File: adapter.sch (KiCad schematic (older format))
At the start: 5 parts, among them CN1 Molex_52602_0579, CN2 CONN_25X2, CN3 CONN_02X22

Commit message: Consolidate all power lines connected on the DC mainboard
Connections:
- net labels removed: +12V_2, +3V3_2, +5V_2, GND2, P.GND, P.GND_2, xA13, xA18, xA21, xB13, xB18, xB21

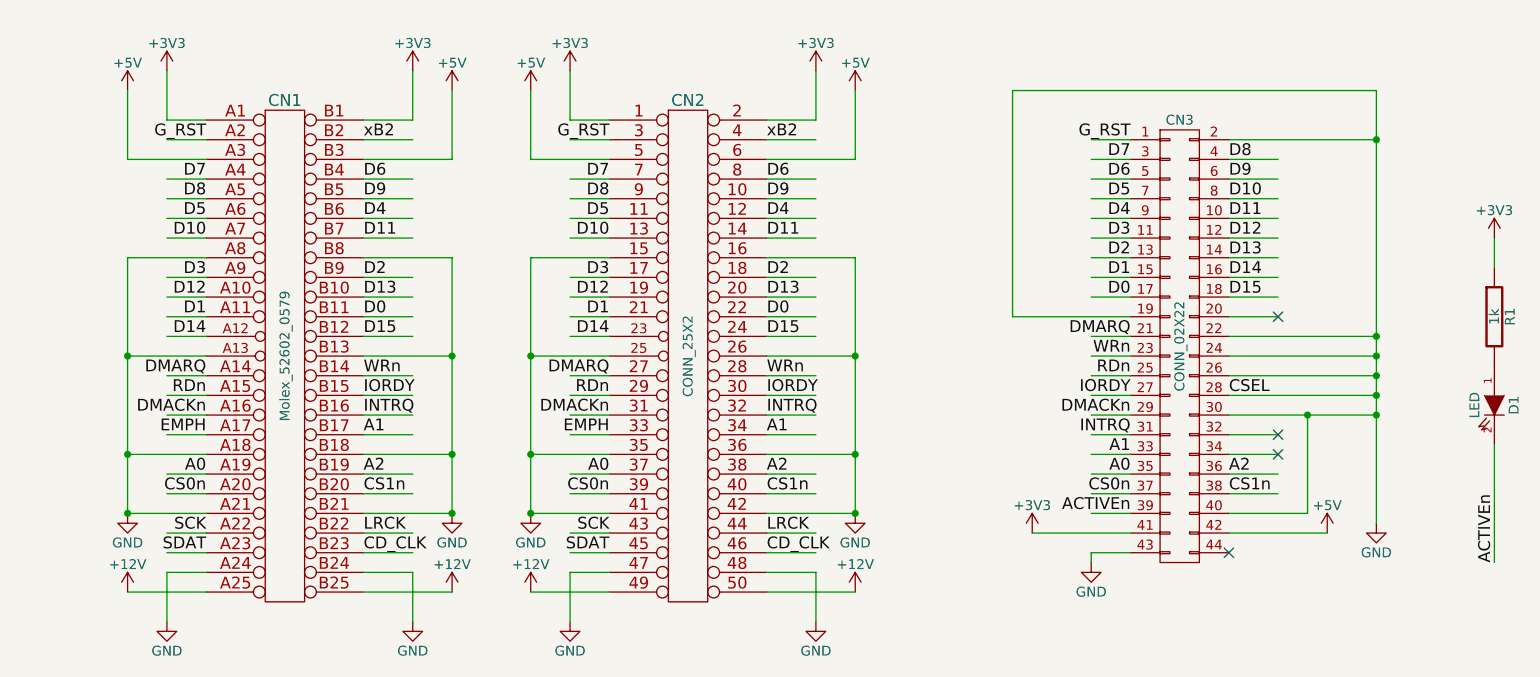
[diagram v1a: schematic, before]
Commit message: Add PWR_FLAG to prevent ERC errors
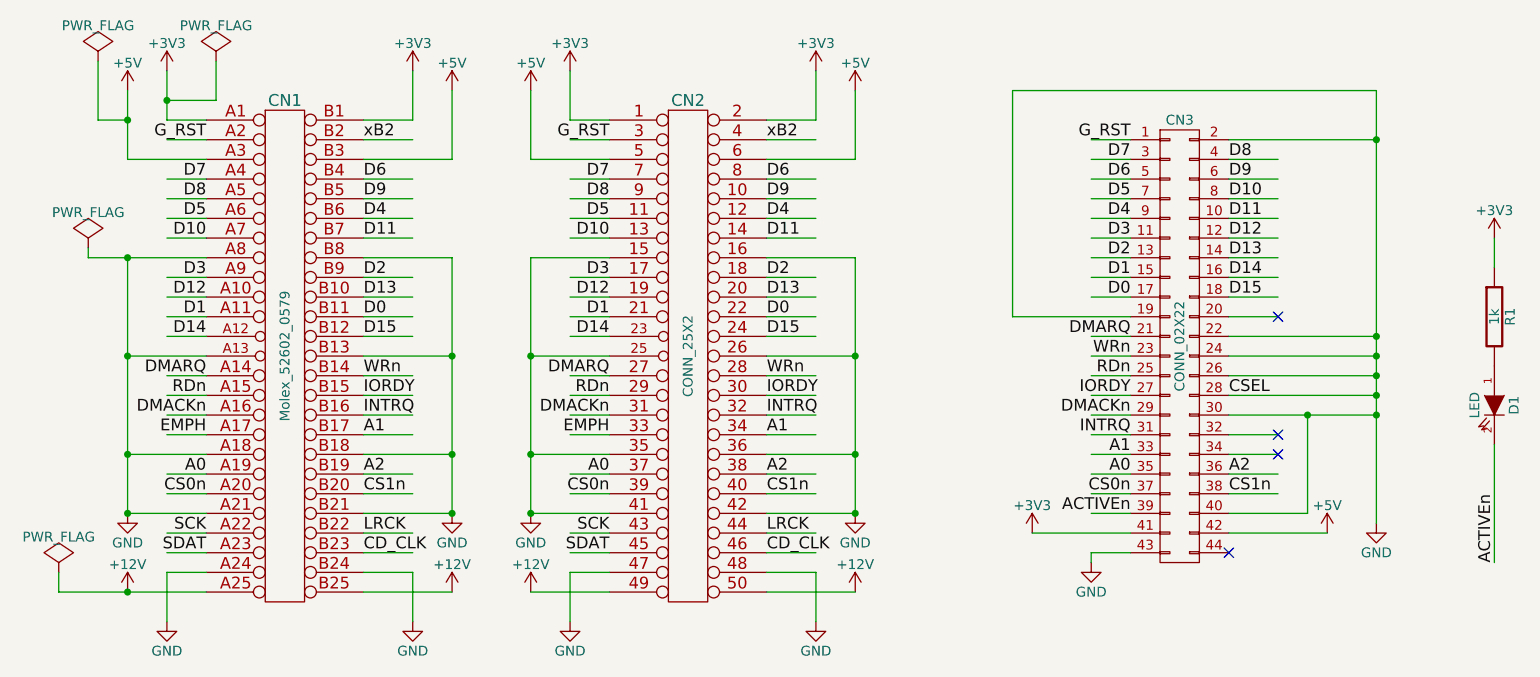
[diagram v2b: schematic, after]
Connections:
- wire segments 166 -> 172
